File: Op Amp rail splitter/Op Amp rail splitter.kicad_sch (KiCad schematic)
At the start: 12 parts, among them J1 Vin, J2 Vout, Q1 BC547, Q2 BC557, U1 LM358

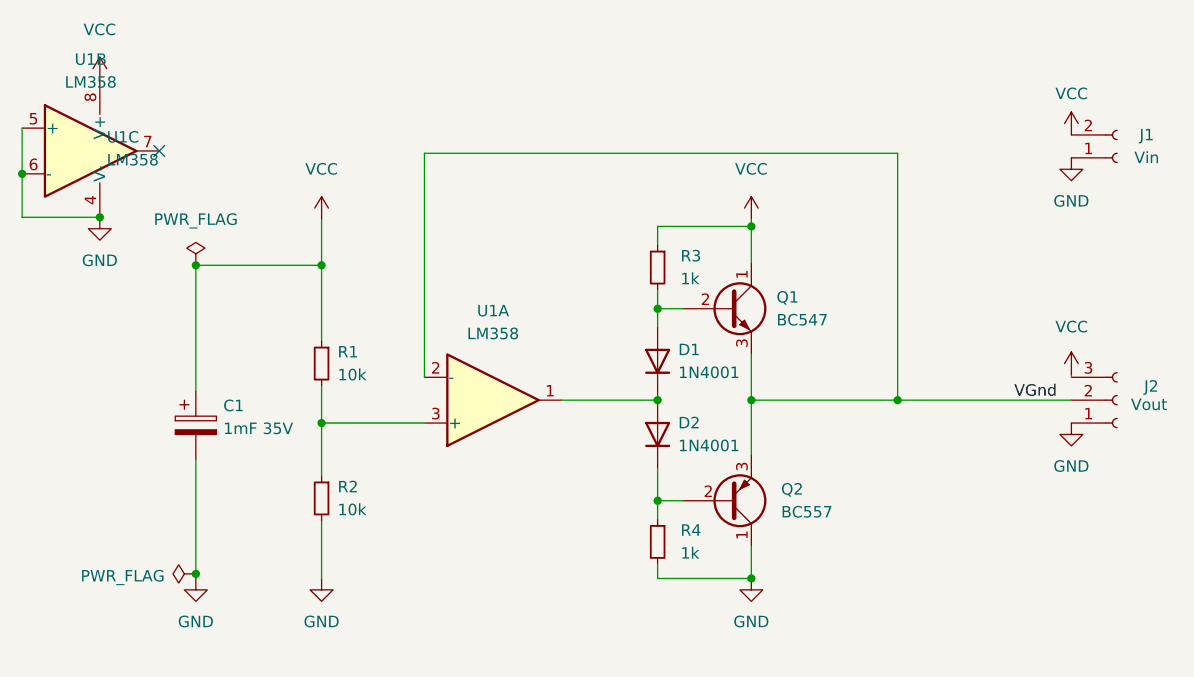
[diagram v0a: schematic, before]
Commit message: Add DAC
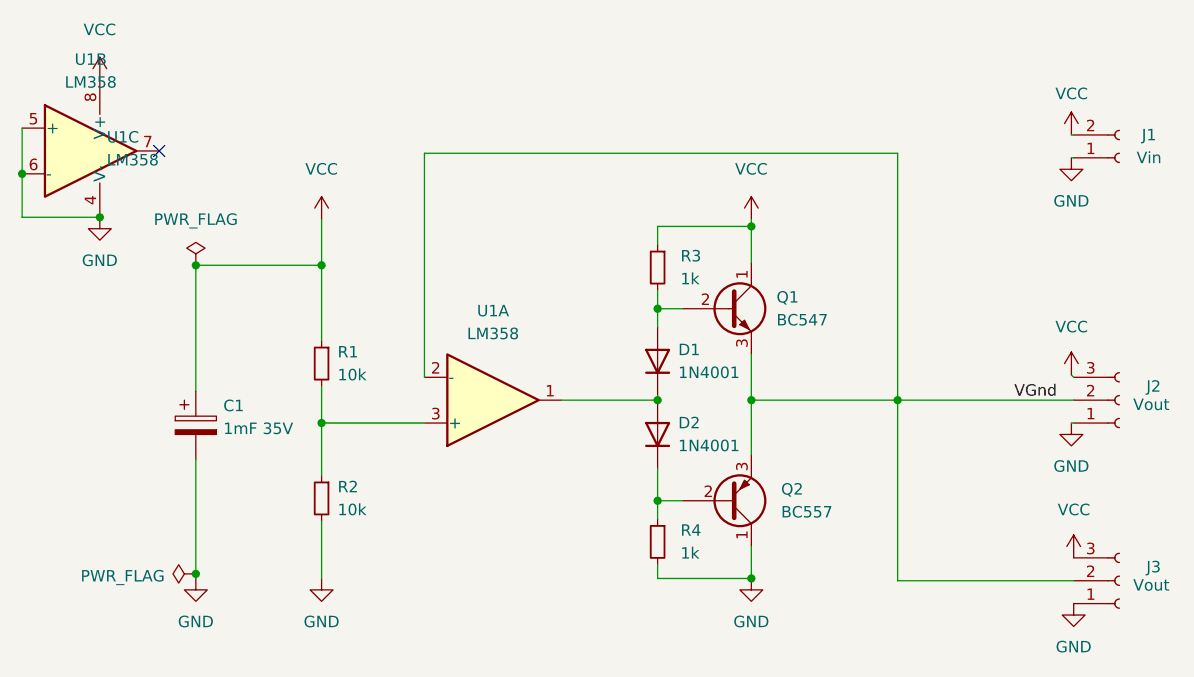
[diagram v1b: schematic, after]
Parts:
- added J3: Vout, Connector_PinHeader_2.54mm:PinHeader_1x03_P2.54mm_Vertical, symbol Connector:Conn_01x03_Female
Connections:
- net GND: now also J3.1 (Pin_1)
- net VCC: now also J3.3 (Pin_3)
- net VGnd: now also J3.2 (Pin_2)
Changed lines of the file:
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@@
     (stroke (width 0) (type default) (color 0 0 0 0))
   )
-  (wire (pts (xy 139.954 50.292) (xy 139.954 50.546))
+  (wire (pts (xy 139.954 50.292) (xy 140.208 50.546))
     (stroke (width 0) (type default) (color 0 0 0 0))
   )
@@
     (stroke (width 0) (type default) (color 0 0 0 0))
   )
-  (wire (pts (xy 120.65 53.086) (xy 139.954 53.086))
+  (wire (pts (xy 120.65 53.086) (xy 140.208 53.086))
     (stroke (width 0) (type default) (color 0 0 0 0))
   )
@@
     (stroke (width 0) (type default) (color 0 0 0 0))
   )
+  (wire (pts (xy 120.65 53.086) (xy 120.65 73.152))
+    (stroke (width 0) (type default) (color 0 0 0 0))
+  )
+  (wire (pts (xy 140.208 26.162) (xy 139.954 26.162))
+    (stroke (width 0) (type default) (color 0 0 0 0))
+  )
   (wire (pts (xy 93.98 35.814) (xy 93.98 33.782))
     (stroke (width 0) (type default) (color 0 0 0 0))
@@
     (stroke (width 0) (type default) (color 0 0 0 0))
   )
+  (wire (pts (xy 140.208 23.622) (xy 139.954 23.622))
+    (stroke (width 0) (type default) (color 0 0 0 0))
+  )
+  (wire (pts (xy 140.208 55.626) (xy 139.954 55.626))
+    (stroke (width 0) (type default) (color 0 0 0 0))
+  )
   (wire (pts (xy 93.98 52.578) (xy 93.98 53.086))
     (stroke (width 0) (type default) (color 0 0 0 0))
@@
   )
   (wire (pts (xy 120.65 53.086) (xy 120.65 25.654))
+    (stroke (width 0) (type default) (color 0 0 0 0))
+  )
+  (wire (pts (xy 120.65 73.152) (xy 140.208 73.152))
     (stroke (width 0) (type default) (color 0 0 0 0))
   )
@@
     (pin "1")
   )
+  (symbol (lib_id "Connector:Conn_01x03_Female") (at 145.288 73.152 0) (mirror x) (unit 1)
+    (in_bom yes) (on_board yes)
+    (property "Reference" "J3" (id 0) (at 149.098 71.628 0))
+    (property "Value" "Vout" (id 1) (at 148.844 73.66 0))
+    (property "Footprint" "Connector_PinHeader_2.54mm:PinHeader_1x03_P2.54mm_Vertical" (id 2) (at 145.288 73.152 0)
+      (effects (font (size 1.27 1.27)) hide)
+    )
+    (property "Datasheet" "~" (id 3) (at 145.288 73.152 0)
+      (effects (font (size 1.27 1.27)) hide)
+    )
+    (pin "1")
+    (pin "2")
+    (pin "3")
+  )
   (symbol (lib_id "Amplifier_Operational:LM358") (at 75.692 53.086 0) (mirror x) (unit 1)
     (in_bom yes) (on_board yes) (fields_autoplaced)
@@
     (pin "3")
   )
-  (symbol (lib_id "Connector:Conn_01x03_Female") (at 145.034 53.086 0) (mirror x) (unit 1)
+  (symbol (lib_id "Connector:Conn_01x03_Female") (at 145.288 53.086 0) (mirror x) (unit 1)
     (in_bom yes) (on_board yes)
-    (property "Reference" "J2" (id 0) (at 148.844 51.562 0))
-    (property "Value" "Vout" (id 1) (at 148.59 53.594 0))
-    (property "Footprint" "Connector_PinHeader_2.54mm:PinHeader_1x03_P2.54mm_Vertical" (id 2) (at 145.034 53.086 0)
-      (effects (font (size 1.27 1.27)) hide)
-    )
-    (property "Datasheet" "~" (id 3) (at 145.034 53.086 0)
+    (property "Reference" "J2" (id 0) (at 149.098 51.562 0))
+    (property "Value" "Vout" (id 1) (at 148.844 53.594 0))
+    (property "Footprint" "Connector_PinHeader_2.54mm:PinHeader_1x03_P2.54mm_Vertical" (id 2) (at 145.288 53.086 0)
+      (effects (font (size 1.27 1.27)) hide)
+    )
+    (property "Datasheet" "~" (id 3) (at 145.288 53.086 0)
       (effects (font (size 1.27 1.27)) hide)
     )
@@
     (pin "3")
   )
+  (symbol (lib_id "power:GND") (at 140.208 75.692 0) (unit 1)
+    (in_bom yes) (on_board yes) (fields_autoplaced)
+    (property "Reference" "#PWR0113" (id 0) (at 140.208 82.042 0)
+      (effects (font (size 1.27 1.27)) hide)
+    )
+    (property "Value" "GND" (id 1) (at 140.208 80.518 0))
+    (property "Footprint" "" (id 2) (at 140.208 75.692 0)
+      (effects (font (size 1.27 1.27)) hide)
+    )
+    (property "Datasheet" "" (id 3) (at 140.208 75.692 0)
+      (effects (font (size 1.27 1.27)) hide)
+    )
+    (pin "1")
+  )
   (symbol (lib_id "Amplifier_Operational:LM358") (at 34.544 25.146 0) (unit 3)
     (in_bom yes) (on_board yes) (fields_autoplaced)
@@
     (pin "4")
     (pin "8")
+  )
+  (symbol (lib_id "power:VCC") (at 140.208 70.612 0) (unit 1)
+    (in_bom yes) (on_board yes)
+    (property "Reference" "#PWR0112" (id 0) (at 140.208 74.422 0)
+      (effects (font (size 1.27 1.27)) hide)
+    )
+    (property "Value" "VCC" (id 1) (at 138.43 65.278 0)
+      (effects (font (size 1.27 1.27)) (justify left))
+    )
+    (property "Footprint" "" (id 2) (at 140.208 70.612 0)
+      (effects (font (size 1.27 1.27)) hide)
+    )
+    (property "Datasheet" "" (id 3) (at 140.208 70.612 0)
+      (effects (font (size 1.27 1.27)) hide)
+    )
+    (pin "1")
   )
   (symbol (lib_id "power:VCC") (at 139.954 50.292 0) (unit 1)
@@
     (pin "7")
   )
-  (symbol (lib_id "Connector:Conn_01x02_Female") (at 145.034 26.162 0) (mirror x) (unit 1)
+  (symbol (lib_id "Connector:Conn_01x02_Female") (at 145.288 26.162 0) (mirror x) (unit 1)
     (in_bom yes) (on_board yes)
-    (property "Reference" "J1" (id 0) (at 148.336 23.622 0))
-    (property "Value" "Vin" (id 1) (at 148.336 26.162 0))
-    (property "Footprint" "Connector_PinHeader_2.54mm:PinHeader_1x02_P2.54mm_Vertical" (id 2) (at 145.034 26.162 0)
-      (effects (font (size 1.27 1.27)) hide)
-    )
-    (property "Datasheet" "~" (id 3) (at 145.034 26.162 0)
+    (property "Reference" "J1" (id 0) (at 148.59 23.622 0))
+    (property "Value" "Vin" (id 1) (at 148.59 26.162 0))
+    (property "Footprint" "Connector_PinHeader_2.54mm:PinHeader_1x02_P2.54mm_Vertical" (id 2) (at 145.288 26.162 0)
+      (effects (font (size 1.27 1.27)) hide)
+    )
+    (property "Datasheet" "~" (id 3) (at 145.288 26.162 0)
       (effects (font (size 1.27 1.27)) hide)
     )
@@
       (reference "#PWR0111") (unit 1) (value "VCC") (footprint "")
     )
+    (path "/af1a5134-bc52-4cc1-b322-f38a966e94c8"
+      (reference "#PWR0112") (unit 1) (value "VCC") (footprint "")
+    )
+    (path "/948e1184-b471-4360-b397-3ae58e62c790"
+      (reference "#PWR0113") (unit 1) (value "GND") (footprint "")
+    )
     (path "/d6e5a1c0-4433-4b37-b508-5b2633e373d4"
       (reference "C1") (unit 1) (value "1mF 35V") (footprint "Capacitor_THT:CP_Radial_D12.5mm_P5.00mm")
@@
       (reference "J2") (unit 1) (value "Vout") (footprint "Connector_PinHeader_2.54mm:PinHeader_1x03_P2.54mm_Vertical")
     )
+    (path "/51e38831-b6fe-409b-99e0-ea87fc114c30"
+      (reference "J3") (unit 1) (value "Vout") (footprint "Connector_PinHeader_2.54mm:PinHeader_1x03_P2.54mm_Vertical")
+    )
     (path "/2dd30b7f-3734-46d0-94cc-1b18069ed498"
